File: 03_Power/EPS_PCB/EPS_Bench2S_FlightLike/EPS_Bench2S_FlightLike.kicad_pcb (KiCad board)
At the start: 2 copper layers, 60 x 60 mm, 10 parts

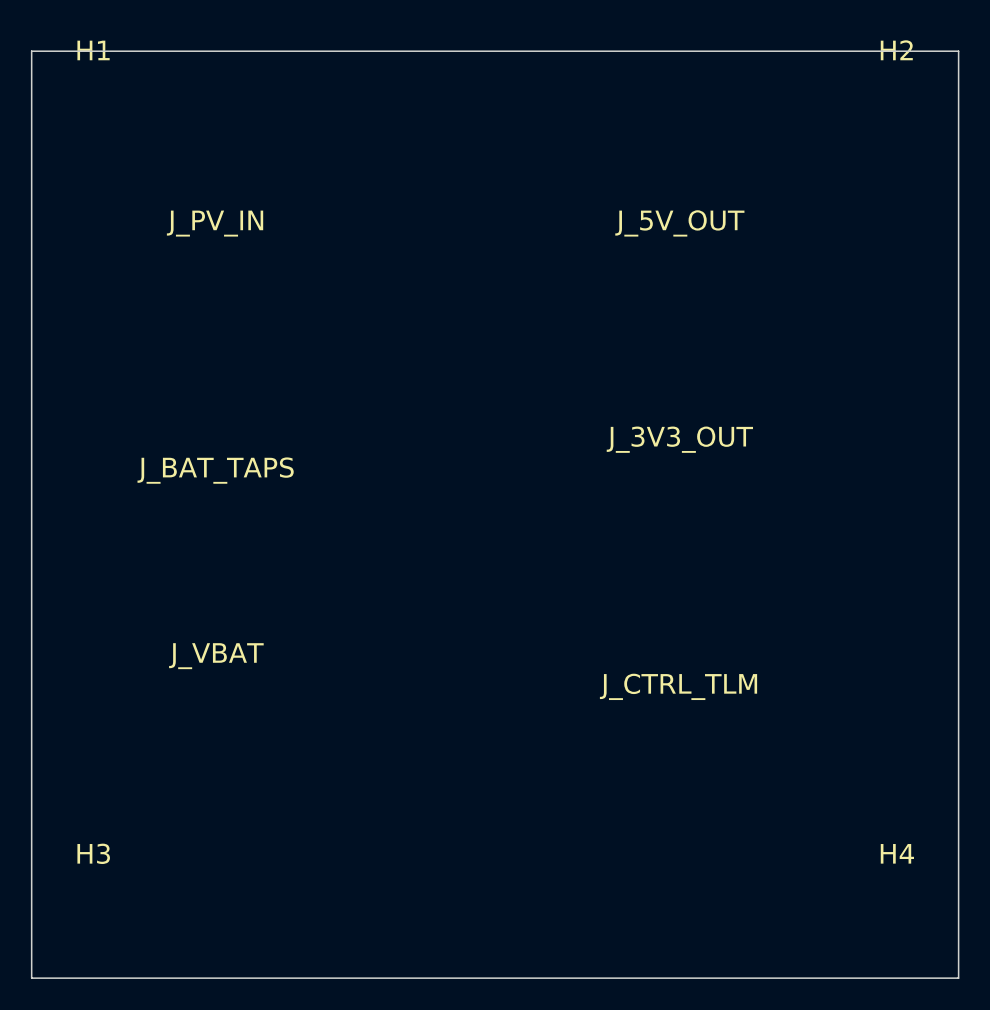
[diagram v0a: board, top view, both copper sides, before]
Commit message: EPS: lock unsafe KiCad placeholder
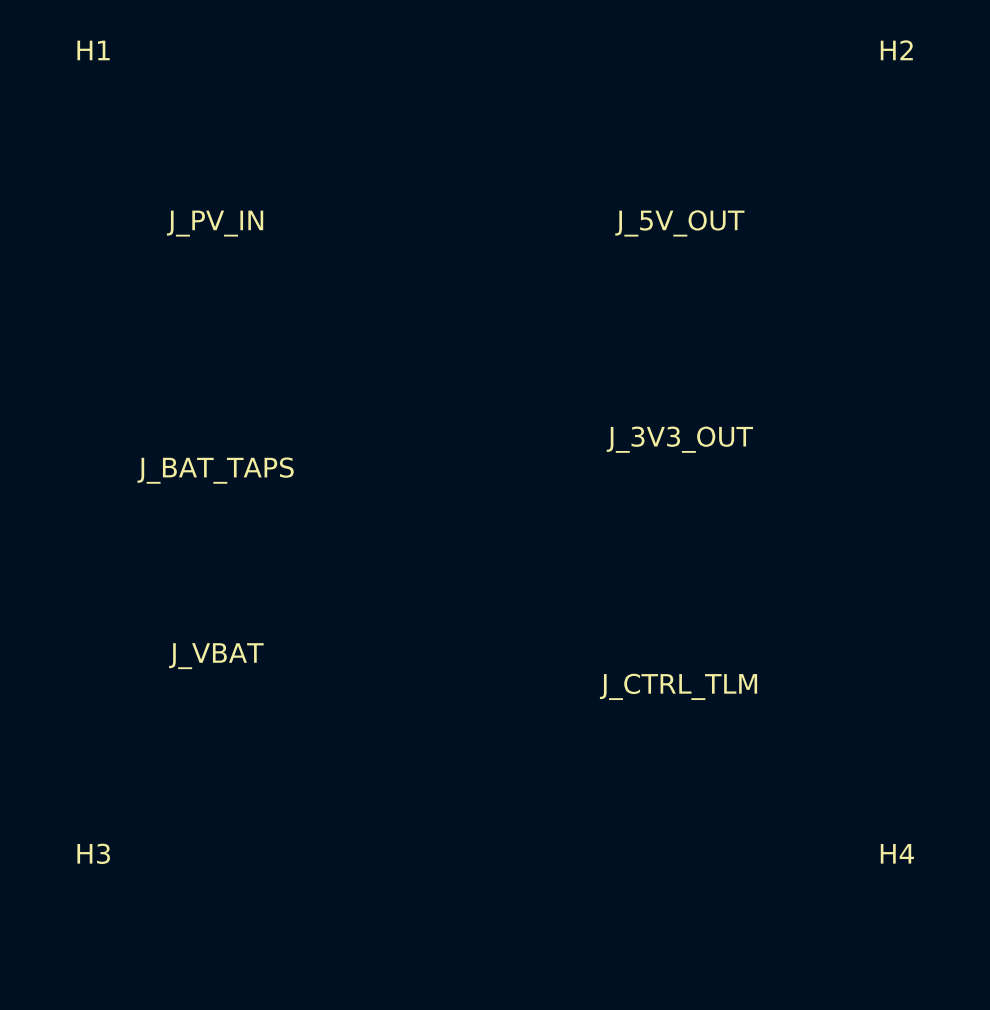
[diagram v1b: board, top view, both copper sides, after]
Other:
- board outline removed
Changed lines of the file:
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@@
 	(net 7 "SW_5V_RF_EN")
 	(net 8 "SW_3V3_OBC_EN")
-	(gr_rect (start 20 20) (end 80 80)
-		(stroke (width 0.1) (type solid))
-		(fill none)
-		(layer "Edge.Cuts")
-	)
 	(footprint "MountingHole:MountingHole_3.2mm_M3"
 		(layer "F.Cu")
